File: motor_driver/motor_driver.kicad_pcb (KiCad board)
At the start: 2 copper layers, 50.8 x 25.4 mm, 36 parts, among them J1 Conn_01x10, J2 Screw_Terminal_01x02, J3 Conn_01x03, J4 GS3, J5 GS3, J6 GS3, J7 Conn_01x06, U1 L298, U2 LM75A

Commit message: routing finished, need to do silkscreen
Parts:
- moved C5 4.76 mm to (122.6, 91.5), turned to 90 degrees
- moved TP5 1.97 mm to (146.8, 95.2)
- moved TP6 1.40 mm to (150.0, 95.2)
- moved R2 1.11 mm to (121.3, 103.1)
- moved TP2 0.40 mm to (124.6, 102.0)
- moved R6 0.26 mm to (140.1, 89.1)
- moved C1 0.25 mm to (157.7, 93.2)
- moved C3 0.25 mm to (157.7, 100.1)
- moved J7 0.06 mm to (139.1, 105.2)
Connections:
- J7 pad 4: Net-(C2-Pad1) -> Net-(C3-Pad2)
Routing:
- net GND: track 0.00 -> 180.6 mm, vias 0 -> 8
- net Net-(J1-Pad2): track 0.00 -> 67.2 mm
- net Net-(C2-Pad1): track 0.00 -> 66.0 mm, vias 0 -> 4
- net Net-(J1-Pad3): track 0.00 -> 62.3 mm, vias 0 -> 4
- net Net-(D3-Pad1): track 0.00 -> 60.5 mm, vias 0 -> 1
- net Net-(D5-Pad1): track 0.00 -> 58.5 mm, vias 0 -> 2
- net Net-(C3-Pad2): track 0.00 -> 56.1 mm, vias 0 -> 1
- net Net-(C1-Pad1): track 0.00 -> 49.9 mm, vias 0 -> 2
- net Net-(J1-Pad4): track 0.00 -> 48.3 mm
- net Net-(J1-Pad6): track 0.00 -> 37.0 mm, vias 0 -> 4
- net Net-(J1-Pad9): track 0.00 -> 36.9 mm, vias 0 -> 1
- net Net-(J1-Pad5): track 0.00 -> 36.5 mm, vias 0 -> 3
- net Net-(J1-Pad10): track 0.00 -> 34.6 mm, vias 0 -> 1
- net Net-(J3-Pad2): track 0.00 -> 30.5 mm
- net Net-(R6-Pad2): track 0.00 -> 9.19 mm
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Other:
- net class Signal added: clearance 0.2032, trace_width 0.2286, via_dia 0.6, via_drill 0.4

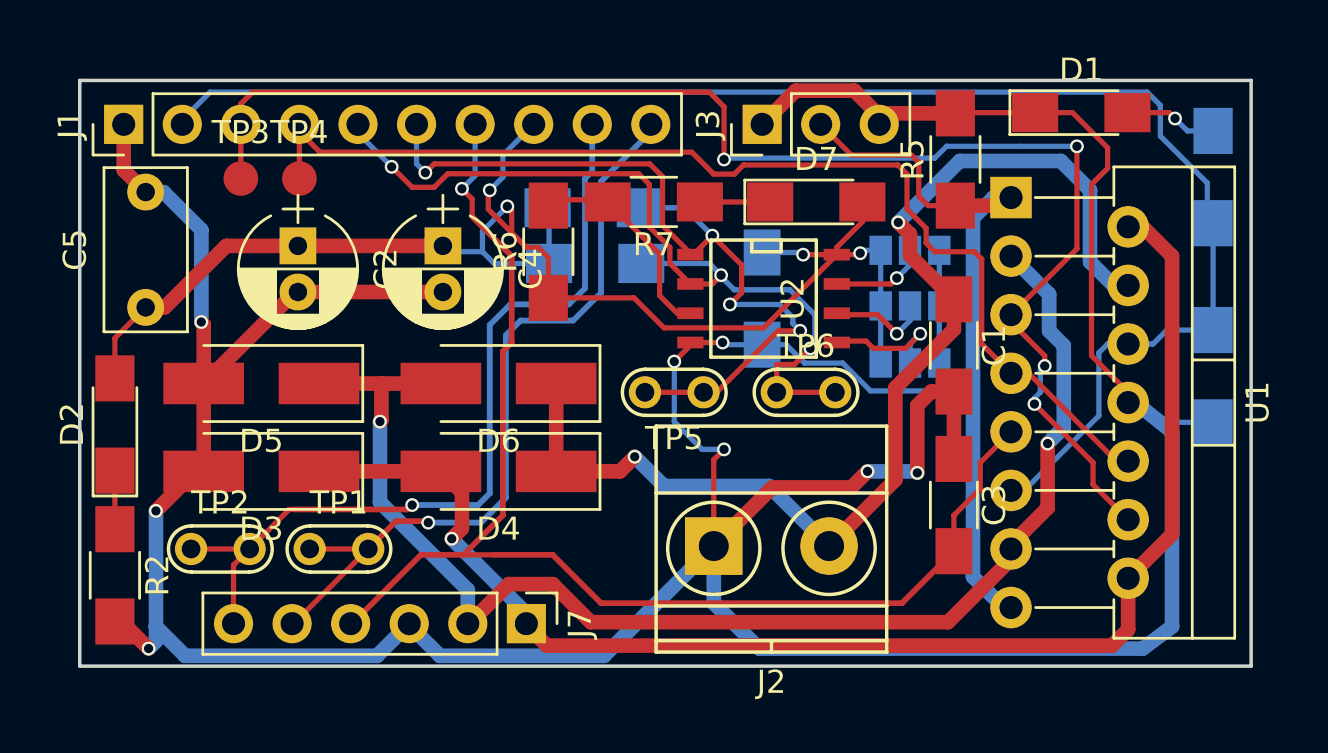
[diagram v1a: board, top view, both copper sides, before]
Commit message: silkscreen finalized
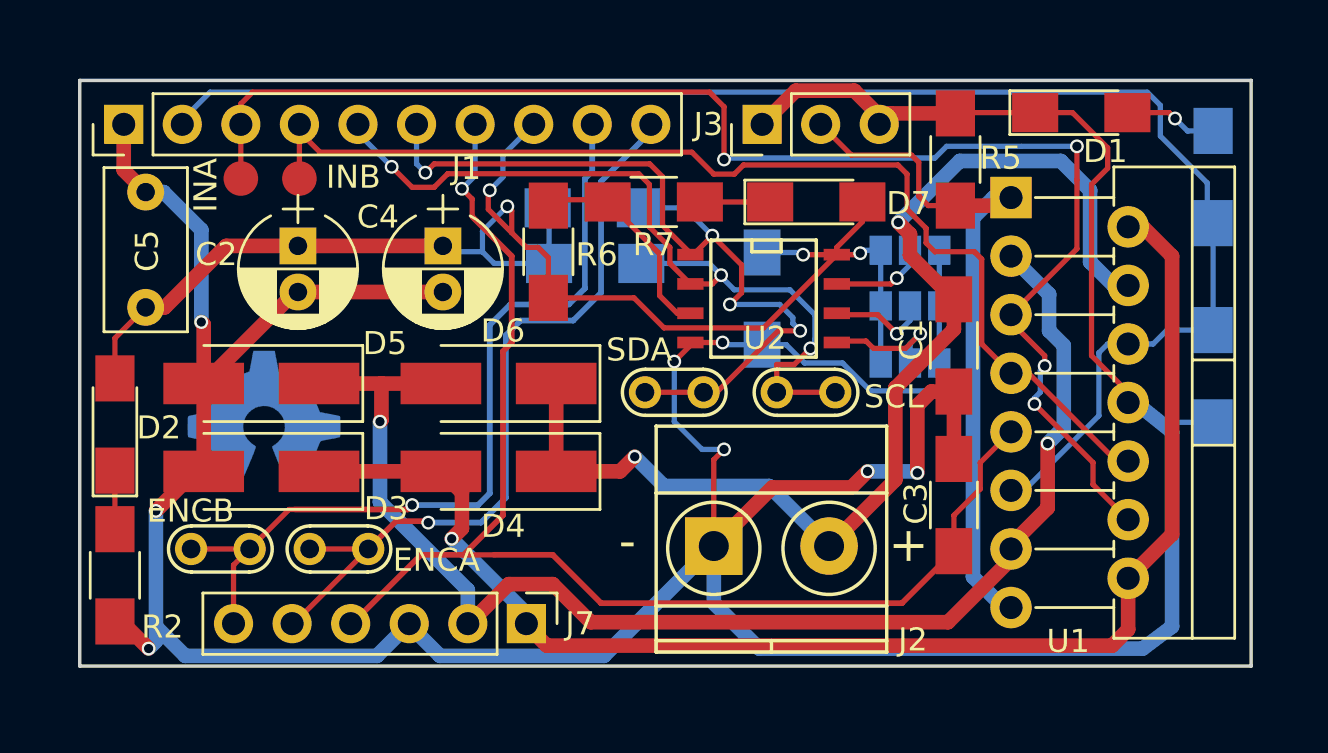
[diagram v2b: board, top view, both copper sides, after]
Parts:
- added REF***: OSHW-Logo_5.7x6mm_SilkScreen, Symbols:OSHW-Logo_5.7x6mm_SilkScreen, B.Cu at (138.5, 100.7)
- added REF***: OSHW-Symbol_6.7x6mm_Copper, Symbols:OSHW-Symbol_6.7x6mm_Copper, B.Cu at (127.8, 96.4)
- renumbered J4 to A0, J5 to A1, J6 to A2, TP1 to ENCA, TP2 to ENCB, TP3 to INA, TP4 to INB, TP6 to SCL, TP5 to SDA
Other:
- board text added: "+"
- board text added: "-"
- board text added: "0"
- board text added: "1"
- board text added: "Cole Mortensen 2018"
- board text added: "L298 Motor Driver & LM75A Temperature Sensor Breakout Board V1.0"
